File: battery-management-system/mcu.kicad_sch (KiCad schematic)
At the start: 44 parts, among them J16 I2C, J17 UART_INTERCONNECT, J18 LEDS, J19 CHARGE/DISCHARGE, J20 UART_USB, Q5 DMN3404L, U10 STC3100, U11 STM32L071CZTx, U7 ARM-JTAG-SWD, U8 AT24C512C, U9 NCT75DR2G

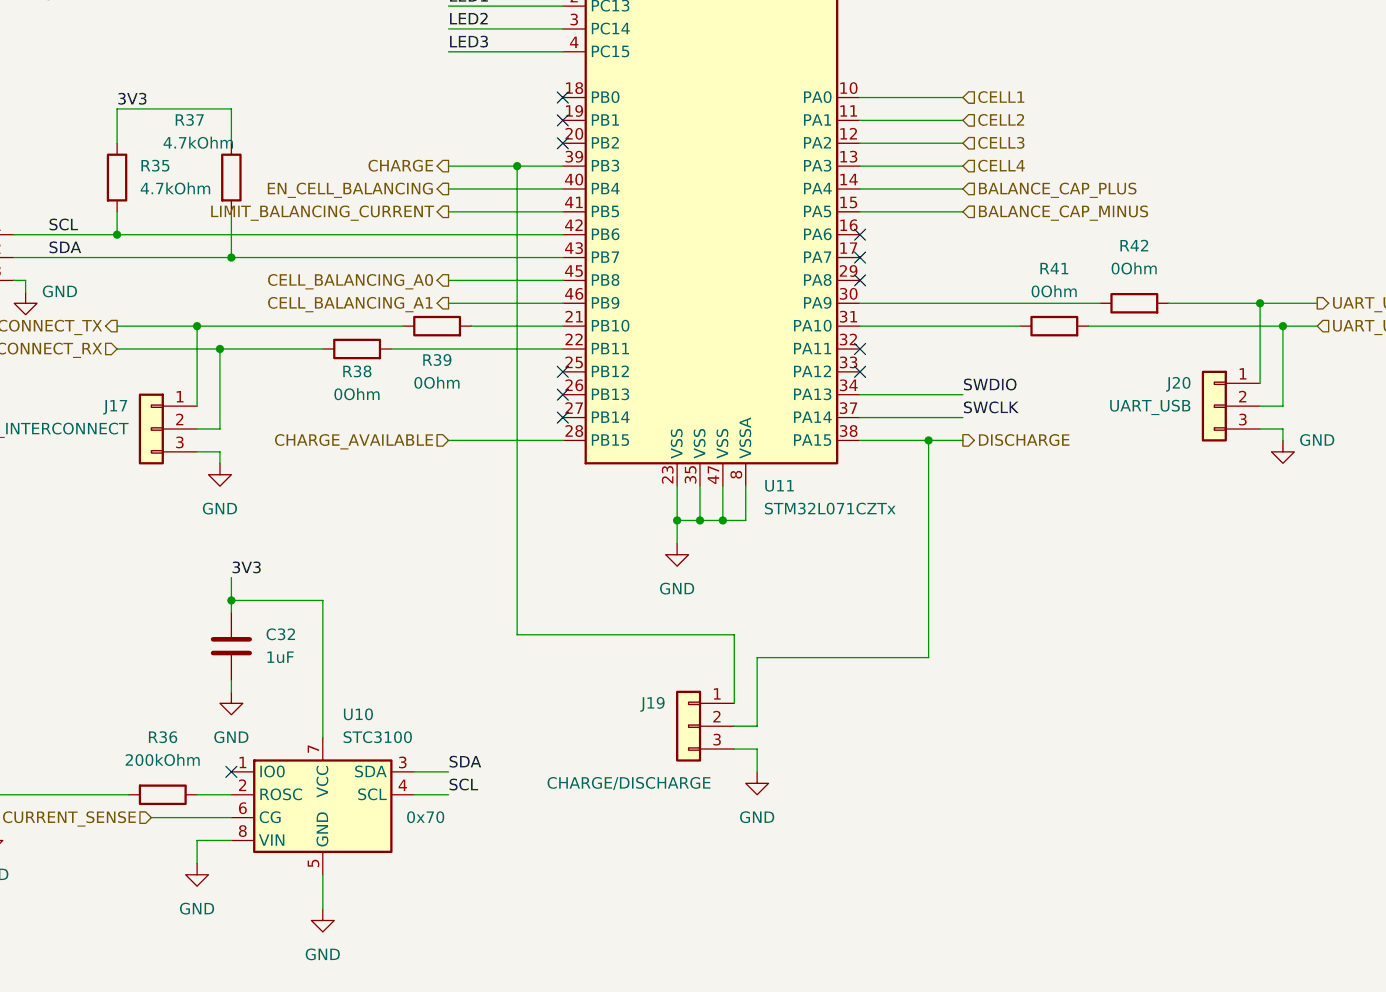
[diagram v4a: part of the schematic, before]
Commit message: finish cell balancing changes
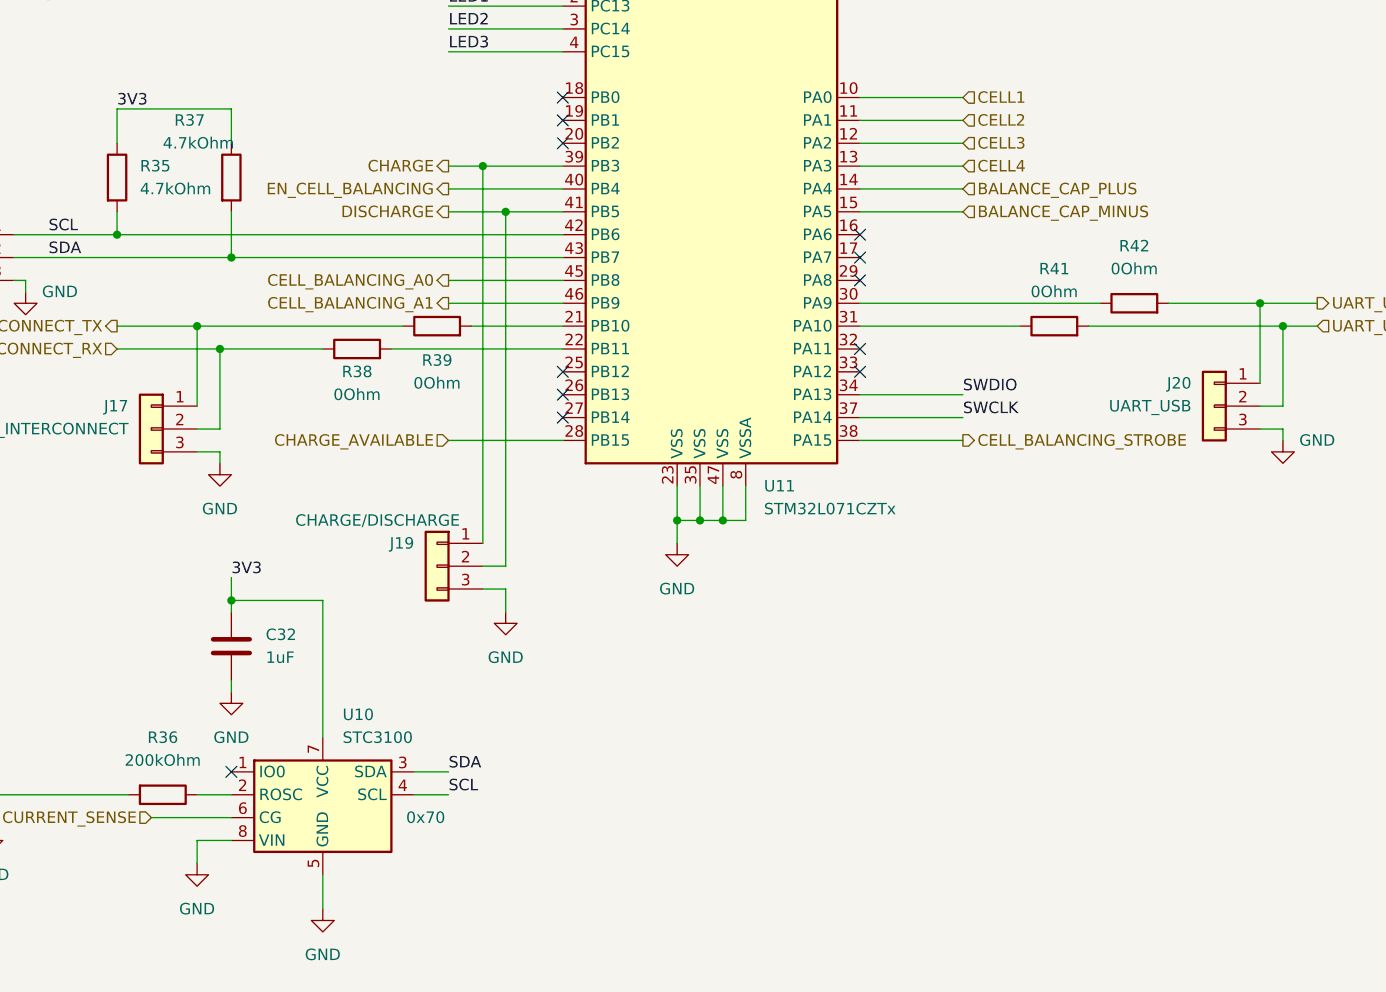
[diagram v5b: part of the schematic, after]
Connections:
- net LIMIT_BALANCING_CURRENT is gone; now on net DISCHARGE: U11.41 (PB5)
- net DISCHARGE: no longer U11.38 (PA15)
- new net CELL_BALANCING_STROBE: U11.38 (PA15)
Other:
- moved on the sheet: J19
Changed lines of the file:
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@@
   (junction (at 90.17 46.99) (diameter 0) (color 0 0 0 0)
   )
-  (junction (at 180.34 73.66) (diameter 0) (color 0 0 0 0)
-  )
   (junction (at 53.34 46.99) (diameter 0) (color 0 0 0 0)
   )
@@
   (junction (at 30.48 110.49) (diameter 0) (color 0 0 0 0)
   )
+  (junction (at 179.07 78.74) (diameter 0) (color 0 0 0 0)
+  )
   (junction (at 36.83 121.92) (diameter 0) (color 0 0 0 0)
   )
@@
   (junction (at 80.01 135.89) (diameter 0) (color 0 0 0 0)
   )
+  (junction (at 176.53 73.66) (diameter 0) (color 0 0 0 0)
+  )
   (junction (at 102.87 31.75) (diameter 0) (color 0 0 0 0)
   )
   (junction (at 116.84 31.75) (diameter 0) (color 0 0 0 0)
-  )
-  (junction (at 226.06 104.14) (diameter 0) (color 0 0 0 0)
   )
   (junction (at 203.2 29.21) (diameter 0) (color 0 0 0 0)
@@
     (stroke (width 0) (type default))
   )
+  (wire (pts (xy 176.53 73.66) (xy 185.42 73.66))
+    (stroke (width 0) (type default))
+  )
   (wire (pts (xy 203.2 29.21) (xy 203.2 33.02))
     (stroke (width 0) (type default))
@@
     (stroke (width 0) (type default))
   )
-  (wire (pts (xy 204.47 135.89) (xy 207.01 135.89))
+  (wire (pts (xy 176.53 118.11) (xy 179.07 118.11))
     (stroke (width 0) (type default))
   )
@@
     (stroke (width 0) (type default))
   )
-  (wire (pts (xy 204.47 125.73) (xy 204.47 133.35))
-    (stroke (width 0) (type default))
-  )
   (wire (pts (xy 218.44 101.6) (xy 229.87 101.6))
     (stroke (width 0) (type default))
@@
     (stroke (width 0) (type default))
   )
-  (wire (pts (xy 226.06 104.14) (xy 229.87 104.14))
+  (wire (pts (xy 218.44 104.14) (xy 229.87 104.14))
     (stroke (width 0) (type default))
   )
@@
     (stroke (width 0) (type default))
   )
-  (wire (pts (xy 207.01 138.43) (xy 204.47 138.43))
+  (wire (pts (xy 179.07 120.65) (xy 176.53 120.65))
     (stroke (width 0) (type default))
   )
@@
     (stroke (width 0) (type default))
   )
-  (wire (pts (xy 180.34 73.66) (xy 185.42 73.66))
+  (wire (pts (xy 172.72 73.66) (xy 176.53 73.66))
     (stroke (width 0) (type default))
   )
@@
     (stroke (width 0) (type default))
   )
-  (wire (pts (xy 172.72 73.66) (xy 180.34 73.66))
-    (stroke (width 0) (type default))
-  )
   (wire (pts (xy 53.34 44.45) (xy 53.34 46.99))
     (stroke (width 0) (type default))
@@
     (stroke (width 0) (type default))
   )
-  (wire (pts (xy 207.01 140.97) (xy 207.01 138.43))
+  (wire (pts (xy 179.07 123.19) (xy 179.07 120.65))
     (stroke (width 0) (type default))
   )
@@
     (stroke (width 0) (type default))
   )
-  (wire (pts (xy 180.34 125.73) (xy 180.34 73.66))
-    (stroke (width 0) (type default))
-  )
   (wire (pts (xy 172.72 60.96) (xy 185.42 60.96))
     (stroke (width 0) (type default))
@@
     (stroke (width 0) (type default))
   )
-  (wire (pts (xy 218.44 104.14) (xy 226.06 104.14))
-    (stroke (width 0) (type default))
-  )
-  (wire (pts (xy 207.01 128.27) (xy 226.06 128.27))
-    (stroke (width 0) (type default))
-  )
   (wire (pts (xy 205.74 109.22) (xy 205.74 113.03))
     (stroke (width 0) (type default))
@@
     (stroke (width 0) (type default))
   )
-  (wire (pts (xy 226.06 128.27) (xy 226.06 104.14))
-    (stroke (width 0) (type default))
-  )
   (wire (pts (xy 27.94 83.82) (xy 33.02 83.82))
     (stroke (width 0) (type default))
@@
     (stroke (width 0) (type default))
   )
+  (wire (pts (xy 179.07 78.74) (xy 179.07 118.11))
+    (stroke (width 0) (type default))
+  )
   (wire (pts (xy 74.93 135.89) (xy 74.93 138.43))
     (stroke (width 0) (type default))
@@
     (stroke (width 0) (type default))
   )
-  (wire (pts (xy 207.01 135.89) (xy 207.01 128.27))
-    (stroke (width 0) (type default))
-  )
   (wire (pts (xy 96.52 81.28) (xy 96.52 83.82))
     (stroke (width 0) (type default))
@@
     (stroke (width 0) (type default))
   )
+  (wire (pts (xy 176.53 73.66) (xy 176.53 115.57))
+    (stroke (width 0) (type default))
+  )
   (wire (pts (xy 172.72 88.9) (xy 185.42 88.9))
     (stroke (width 0) (type default))
@@
     (stroke (width 0) (type default))
   )
+  (wire (pts (xy 179.07 78.74) (xy 185.42 78.74))
+    (stroke (width 0) (type default))
+  )
   (wire (pts (xy 109.22 151.13) (xy 109.22 154.94))
     (stroke (width 0) (type default))
   )
-  (wire (pts (xy 172.72 78.74) (xy 185.42 78.74))
+  (wire (pts (xy 172.72 78.74) (xy 179.07 78.74))
     (stroke (width 0) (type default))
   )
   (wire (pts (xy 49.53 115.57) (xy 49.53 110.49))
-    (stroke (width 0) (type default))
-  )
-  (wire (pts (xy 204.47 125.73) (xy 180.34 125.73))
     (stroke (width 0) (type default))
   )
@@
     (effects (font (size 1.27 1.27)) (justify left))
   )
+  (hierarchical_label "DISCHARGE" (shape output) (at 172.72 78.74 180) (fields_autoplaced)
+    (effects (font (size 1.27 1.27)) (justify right))
+  )
+  (hierarchical_label "CELL_BALANCING_STROBE" (shape output) (at 229.87 104.14 0) (fields_autoplaced)
+    (effects (font (size 1.27 1.27)) (justify left))
+  )
   (hierarchical_label "SDA" (shape bidirectional) (at 115.57 120.65 0) (fields_autoplaced)
     (effects (font (size 1.27 1.27)) (justify left))
@@
     (effects (font (size 1.27 1.27)) (justify right))
   )
-  (hierarchical_label "LIMIT_BALANCING_CURRENT" (shape output) (at 172.72 78.74 180) (fields_autoplaced)
-    (effects (font (size 1.27 1.27)) (justify right))
-  )
   (hierarchical_label "CELL4" (shape input) (at 229.87 73.66 0) (fields_autoplaced)
     (effects (font (size 1.27 1.27)) (justify left))
@@
   (hierarchical_label "CURRENT_SENSE" (shape input) (at 139.7 146.05 180) (fields_autoplaced)
     (effects (font (size 1.27 1.27)) (justify right))
-  )
-  (hierarchical_label "DISCHARGE" (shape output) (at 229.87 104.14 0) (fields_autoplaced)
-    (effects (font (size 1.27 1.27)) (justify left))
   )
   (hierarchical_label "CELL2" (shape input) (at 229.87 68.58 0) (fields_autoplaced)
@@
     )
   )
-  (symbol (lib_id "power:GND") (at 207.01 140.97 0) (unit 1)
-    (in_bom yes) (on_board yes) (dnp no) (fields_autoplaced)
-    (property "Reference" "#PWR064" (at 207.01 147.32 0)
-      (effects (font (size 1.27 1.27)) hide)
-    )
-    (property "Value" "GND" (at 207.01 146.05 0)
-      (effects (font (size 1.27 1.27)))
-    )
-    (property "Footprint" "" (at 207.01 140.97 0)
-      (effects (font (size 1.27 1.27)) hide)
-    )
-    (property "Datasheet" "" (at 207.01 140.97 0)
+  (symbol (lib_id "power:GND") (at 179.07 123.19 0) (unit 1)
+    (in_bom yes) (on_board yes) (dnp no) (fields_autoplaced)
+    (property "Reference" "#PWR064" (at 179.07 129.54 0)
+      (effects (font (size 1.27 1.27)) hide)
+    )
+    (property "Value" "GND" (at 179.07 128.27 0)
+      (effects (font (size 1.27 1.27)))
+    )
+    (property "Footprint" "" (at 179.07 123.19 0)
+      (effects (font (size 1.27 1.27)) hide)
+    )
+    (property "Datasheet" "" (at 179.07 123.19 0)
       (effects (font (size 1.27 1.27)) hide)
     )
@@
     )
   )
-  (symbol (lib_id "benediktibk:Conn_01x03") (at 199.39 135.89 0) (mirror y) (unit 1)
+  (symbol (lib_id "benediktibk:Conn_01x03") (at 171.45 118.11 0) (mirror y) (unit 1)
     (in_bom yes) (on_board yes) (dnp no)
-    (property "Reference" "J19" (at 196.85 133.35 0)
-      (effects (font (size 1.27 1.27)) (justify left))
-    )
-    (property "Value" "CHARGE/DISCHARGE" (at 201.93 142.24 0)
-      (effects (font (size 1.27 1.27)) (justify left))
-    )
-    (property "Footprint" "benediktibk:PinHeader_1x03_P2.54mm_Vertical" (at 199.39 135.89 0)
-      (effects (font (size 1.27 1.27)) hide)
-    )
-    (property "Datasheet" "~" (at 199.39 135.89 0)
-      (effects (font (size 1.27 1.27)) hide)
-    )
-    (property "RS order number" "251-8092" (at 199.39 135.89 0)
-      (effects (font (size 1.27 1.27)) hide)
-    )
+    (property "Reference" "J19" (at 168.91 115.57 0)
+      (effects (font (size 1.27 1.27)) (justify left))
+    )
+    (property "Value" "CHARGE/DISCHARGE" (at 173.99 113.03 0)
+      (effects (font (size 1.27 1.27)) (justify left))
+    )
+    (property "Footprint" "benediktibk:PinHeader_1x03_P2.54mm_Vertical" (at 171.45 118.11 0)
+      (effects (font (size 1.27 1.27)) hide)
+    )
+    (property "Datasheet" "~" (at 171.45 118.11 0)
+      (effects (font (size 1.27 1.27)) hide)
+    )
+    (property "RS order number" "251-8092" (at 171.45 118.11 0)
+      (effects (font (size 1.27 1.27)) hide)
+    )
